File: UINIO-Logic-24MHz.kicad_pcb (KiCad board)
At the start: 2 copper layers, 52 x 25.4 mm, 55 parts, among them J1 Conn_01x10_Pin, U1 AT24CS64-XHM, U2 74HC245C, U3 ME6211C33M5G-N, U4 CY7C68013A-56LTX, Y1 24MHz

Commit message: update hardware
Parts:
- removed F1: 60V 1A, Fuse:Fuse_1206_3216Metric
- removed HOLE1, HOLE2, HOLE3, HOLE4: Hole-2mm, Uinio:Hole-2mm
- removed J1: Conn_01x10_Pin, Connector_PinHeader_2.54mm:PinHeader_1x10_P2.54mm_Vertical
- removed Y1: 24MHz, Crystal:Crystal_SMD_3225-4Pin_3.2x2.5mm
- added Y2: Crystal, Crystal:Crystal_SMD_HC49-SD, F.Cu at (143.8, 57.0)
- U1: footprint Package_SO:TSSOP-8_4.4x3mm_P0.65mm -> Package_SO:SO-8_3.9x4.9mm_P1.27mm
- U3: value ME6211C33M5G-N -> AP2127N-3.3; footprint Uinio:SOT-23-5_L3.0-W1.7-P0.95-LS2.8-BR -> Package_TO_SOT_SMD:SOT-23
- moved R1 57.5 mm to (137.9, 61.4)
- moved R13 56.7 mm to (143.7, 61.4), turned to 0 degrees
- moved R14 55.2 mm to (143.7, 63.4), turned to 0 degrees
- moved C1 55.2 mm to (150.1, 61.6), turned to 0 degrees
- moved R2 54.6 mm to (137.9, 63.4)
- moved R15 53.8 mm to (143.7, 65.3), turned to 0 degrees
- moved R16 52.5 mm to (143.7, 67.3), turned to 0 degrees
- moved D5 52.0 mm to (159.6, 61.6), turned to 0 degrees
- moved C2 51.7 mm to (150.1, 64.1), turned to 0 degrees
- moved R3 51.7 mm to (137.9, 65.3)
- moved C3 50.5 mm to (153.5, 61.4)
- moved D1 49.8 mm to (158.4, 71.7), turned to 0 degrees
- moved R4 48.9 mm to (137.9, 67.3)
- moved R7 48.4 mm to (140.8, 61.4)
- moved R17 48.0 mm to (143.7, 69.3)
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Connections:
- C2 pad 2: Net-(U3-Vout) -> +3.3V
- R1 pad 2: Net-(J1-Pin_9) -> unconnected-(R1-Pad2)
- R2 pad 2: Net-(J1-Pin_8) -> unconnected-(R2-Pad2)
- R3 pad 2: Net-(J1-Pin_7) -> unconnected-(R3-Pad2)
- R4 pad 2: Net-(J1-Pin_6) -> unconnected-(R4-Pad2)
- R5 pad 2: Net-(J1-Pin_5) -> unconnected-(R5-Pad2)
- R6 pad 2: Net-(J1-Pin_4) -> unconnected-(R6-Pad2)
- R7 pad 2: Net-(J1-Pin_3) -> unconnected-(R7-Pad2)
- R8 pad 2: Net-(J1-Pin_2) -> unconnected-(R8-Pad2)
- U3 pad 1: +5V -> GND
- U3 pad 2: GND -> +3.3V
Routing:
- net +3.3V: track 167.8 -> 0.00 mm, vias 12 -> 0
- net /USB_Data-: track 29.3 -> 0.00 mm
- net /USB_Data+: track 27.9 -> 0.00 mm, vias 2 -> 0
- net GND: track 24.0 -> 0.00 mm, vias 59 -> 0
- net Net-(U4-XTALIN): track 24.0 -> 0.00 mm
- net Net-(U4-XTALOUT): track 19.4 -> 0.00 mm
- net /INPUT4: track 16.8 -> 0.00 mm, vias 2 -> 0
- net /INPUT3: track 15.8 -> 0.00 mm, vias 2 -> 0
- net /INPUT5: track 15.3 -> 0.00 mm, vias 2 -> 0
- net /INPUT2: track 15.0 -> 0.00 mm, vias 2 -> 0
- net /INPUT6: track 14.4 -> 0.00 mm, vias 2 -> 0
- net /INPUT1: track 14.4 -> 0.00 mm, vias 2 -> 0
- net /INPUT7: track 13.4 -> 0.00 mm, vias 2 -> 0
- net /INPUT8: track 12.5 -> 0.00 mm, vias 2 -> 0
- net Net-(U4-PA0/~{INT0}): track 12.2 -> 0.00 mm
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- removed copper zone on B.Cu, net +3.3V
- removed copper zone on F.Cu, net +3.3V
- removed copper zone on B.Cu, net +5V
- removed copper zone on F.Cu, net +5V
- removed copper zone on F.Cu, net Net-(U3-Vout)
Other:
- board text removed: "CH0"
- board text removed: "CH1"
- board text removed: "CH2"
- board text removed: "CH3"
- board text removed: "CH4"
- board text removed: "CH5"
- board text removed: "CH6"
- board text removed: "CH7"
- board text removed: "GND"
- board text removed: "PA0"
- board text removed: "PA1"
- board text removed: "Power"
- board text removed: "UINIO Logic 24MHz"
- board text removed: "UINIO-Logic-24MHz"
- board text removed: "UinIO.com"
- board text removed: "Version 5.0.0"

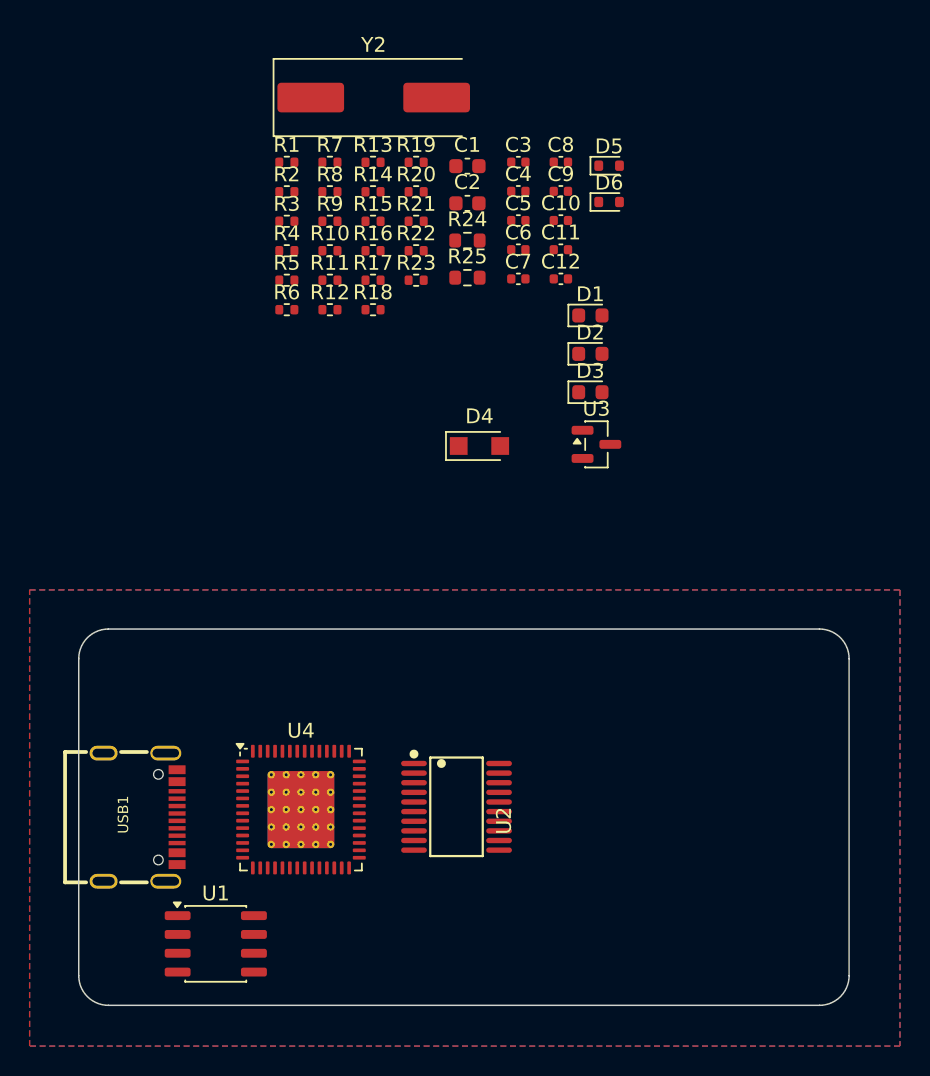
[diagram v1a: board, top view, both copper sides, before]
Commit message: update sch & brd with saleae clone hardware
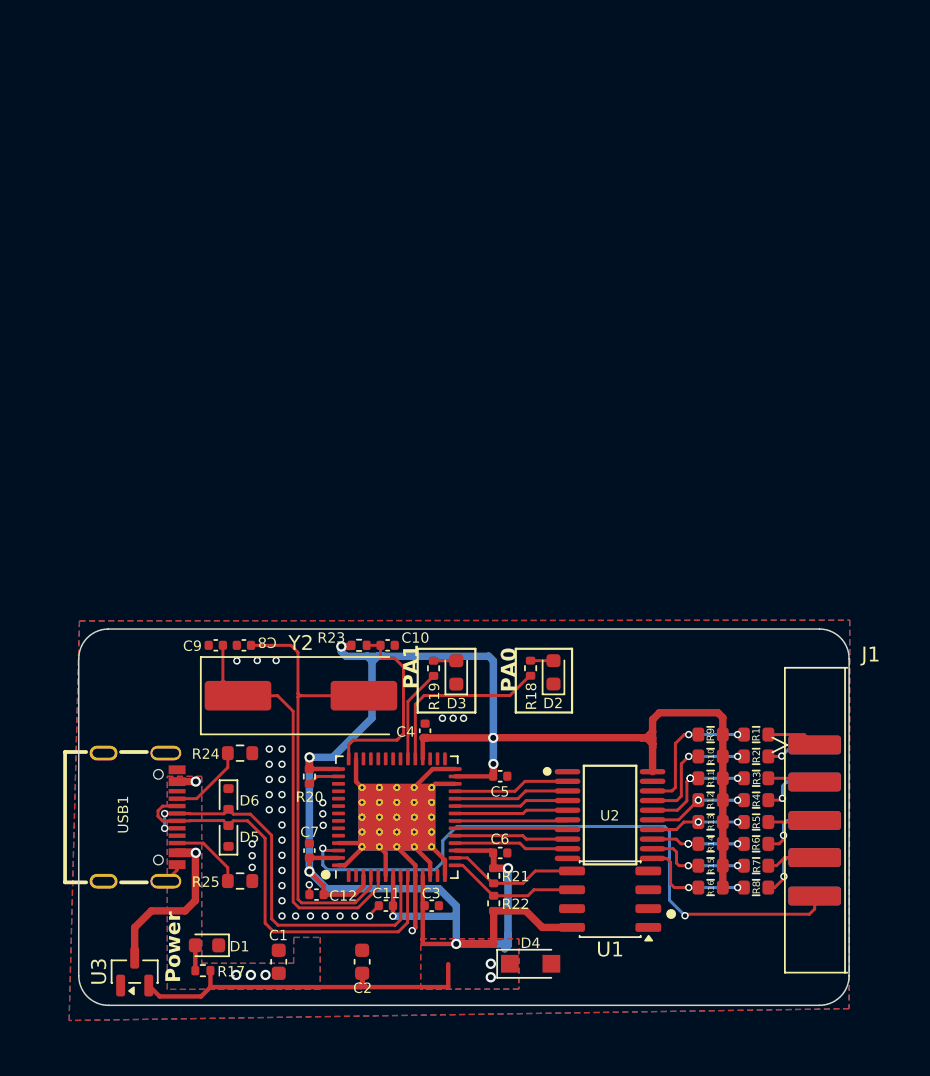
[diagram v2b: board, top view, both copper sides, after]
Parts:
- added J1: Conn_01x10_Pin, Uinio:IDC-Header_2x05_P2.54mm_EdgeMount, F.Cu at (171.1, 100.7)
- R1, R10, R11, R12, R13, R14, R15, R16, R2, R3, R4, R5, R6, R7, R8, R9: footprint Resistor_SMD:R_0402_1005Metric -> Resistor_SMD:R_0603_1608Metric
- moved R7 55.5 mm to (169.6, 108.8), turned to 180 degrees
- moved C1 55.2 mm to (137.3, 115.3), turned to -90 degrees
- moved R8 55.1 mm to (169.6, 110.3), turned to 180 degrees
- moved D5 52.0 mm to (133.9, 106.8), turned to 90 degrees
- moved C2 51.7 mm to (143.0, 115.3), turned to -90 degrees
- moved C3 50.5 mm to (147.7, 111.5)
- moved R13 50.0 mm to (166.5, 105.9)
- moved R1 50.0 mm to (169.6, 100.0), turned to 180 degrees
- moved D1 49.8 mm to (132.5, 114.2), turned to 180 degrees
- moved R14 49.6 mm to (166.5, 107.4)
- moved R2 49.6 mm to (169.6, 101.5), turned to 180 degrees
- moved R3 49.2 mm to (169.6, 103.0), turned to 180 degrees
- moved R15 49.1 mm to (166.5, 108.8)
- moved R4 48.8 mm to (169.6, 104.4), turned to 180 degrees
- moved R16 48.7 mm to (166.5, 110.3)
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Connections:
- R1 pad 1: /INPUT8 -> Net-(J1-Pin_1)
- R1 pad 2: unconnected-(R1-Pad2) -> /INPUT1
- R10 pad 1: +3.3V -> /INPUT2
- R10 pad 2: /INPUT2 -> +3.3V
- R11 pad 1: +3.3V -> /INPUT3
- R11 pad 2: /INPUT3 -> +3.3V
- R12 pad 1: +3.3V -> /INPUT4
- R12 pad 2: /INPUT4 -> +3.3V
- R13 pad 1: +3.3V -> /INPUT5
- R13 pad 2: /INPUT5 -> +3.3V
- R14 pad 1: +3.3V -> /INPUT6
- R14 pad 2: /INPUT6 -> +3.3V
- R15 pad 1: +3.3V -> /INPUT7
- R15 pad 2: /INPUT7 -> +3.3V
- R16 pad 1: +3.3V -> /INPUT8
- R16 pad 2: /INPUT8 -> +3.3V
- R2 pad 1: /INPUT7 -> Net-(J1-Pin_2)
- R2 pad 2: unconnected-(R2-Pad2) -> /INPUT2
- R3 pad 1: /INPUT6 -> Net-(J1-Pin_3)
- R3 pad 2: unconnected-(R3-Pad2) -> /INPUT3
- R4 pad 1: /INPUT5 -> Net-(J1-Pin_4)
- R4 pad 2: unconnected-(R4-Pad2) -> /INPUT4
- R5 pad 1: /INPUT4 -> Net-(J1-Pin_5)
- R5 pad 2: unconnected-(R5-Pad2) -> /INPUT5
- R6 pad 1: /INPUT3 -> Net-(J1-Pin_6)
- R6 pad 2: unconnected-(R6-Pad2) -> /INPUT6
- R7 pad 1: /INPUT2 -> Net-(J1-Pin_7)
- R7 pad 2: unconnected-(R7-Pad2) -> /INPUT7
- R8 pad 1: /INPUT1 -> Net-(J1-Pin_8)
- R8 pad 2: unconnected-(R8-Pad2) -> /INPUT8
- R9 pad 1: +3.3V -> /INPUT1
- R9 pad 2: /INPUT1 -> +3.3V
- U4 pad 54: unconnected-(U4-CLKOUT-Pad54) -> /CLK
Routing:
- net +3.3V: track 0.00 -> 169.1 mm, vias 0 -> 10
- net /CLK: track 0.00 -> 43.9 mm, vias 0 -> 2
- net Net-(U4-XTALOUT): track 0.00 -> 31.1 mm
- net /USB_Data-: track 0.00 -> 29.3 mm
- net Net-(U4-XTALIN): track 0.00 -> 28.2 mm
- net /USB_Data+: track 0.00 -> 27.9 mm, vias 0 -> 2
- net GND: track 0.00 -> 27.1 mm, vias 0 -> 37
- net Net-(U4-~{RESET}): track 0.00 -> 13.0 mm
- net +5V: track 0.00 -> 12.6 mm, vias 0 -> 5
- net Net-(U4-PA0/~{INT0}): track 0.00 -> 12.2 mm
- net /INPUT1: track 0.00 -> 10.8 mm, vias 0 -> 2
- net /INPUT2: track 0.00 -> 9.35 mm, vias 0 -> 2
- net /I2C_SDA: track 0.00 -> 8.88 mm
- net /I2C_SCL: track 0.00 -> 8.87 mm
- net /INPUT8: track 0.00 -> 8.48 mm, vias 0 -> 2
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- added copper zone on B.Cu, net +3.3V
- added copper zone on F.Cu, net +3.3V
- added copper zone on B.Cu, net +5V
- added copper zone on F.Cu, net +5V
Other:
- board text added: "PA0"
- board text added: "PA1"
- board text added: "Power"

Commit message: fix some routing
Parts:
- removed C12: 0.1uF, Capacitor_SMD:C_0402_1005Metric
- removed D4: 1N4007, Diode_SMD:Nexperia_CFP3_SOD-123W
- added JP1: ~, Uinio:SolderJumper-2_Open_RoundedPad_small, F.Cu at (149.2, 101.8)
- added JP10: ~, Uinio:SolderJumper-2_Open_RoundedPad_small, F.Cu at (139.8, 113.5)
- added JP2: ~, Uinio:SolderJumper-2_Open_RoundedPad_small, F.Cu at (149.2, 102.5)
- added JP3: ~, Uinio:SolderJumper-2_Open_RoundedPad_small, F.Cu at (149.2, 103.2)
- added JP4: ~, Uinio:SolderJumper-2_Open_RoundedPad_small, F.Cu at (149.2, 103.9)
- added JP5: ~, Uinio:SolderJumper-2_Open_RoundedPad_small, F.Cu at (149.2, 104.6)
- added JP6: ~, Uinio:SolderJumper-2_Open_RoundedPad_small, F.Cu at (149.2, 105.3)
- added JP7: ~, Uinio:SolderJumper-2_Open_RoundedPad_small, F.Cu at (149.2, 106.0)
- added JP8: ~, Uinio:SolderJumper-2_Open_RoundedPad_small, F.Cu at (149.2, 106.7)
- added JP9: ~, Uinio:SolderJumper-2_Open_RoundedPad_small, F.Cu at (139.8, 112.8)
- C10, C11, C3, C4, C5, C6, C7, C8, C9: footprint Capacitor_SMD:C_0402_1005Metric -> Capacitor_SMD:C_0603_1608Metric
- D1, D2, D3: footprint LED_SMD:LED_0603_1608Metric -> LED_SMD:LED_0805_2012Metric
- D5, D6: moved to B.Cu
- R17, R18, R19, R20, R21, R22, R23: footprint Resistor_SMD:R_0402_1005Metric -> Resistor_SMD:R_0603_1608Metric
- U4: footprint Package_DFN_QFN:QFN-56-1EP_8x8mm_P0.5mm_EP4.5x5.2mm_ThermalVias_TopTented -> Package_DFN_QFN:QFN-56-1EP_8x8mm_P0.5mm_EP4.5x5.2mm_ThermalVias
- USB1: footprint Uinio:USB-C-SMD_TYPEC-304J-BCP16 -> Connector_USB:USB_C_Receptacle_GCT_USB4105-xx-A_16P_TopMnt_Horizontal
- Y2: footprint Crystal:Crystal_SMD_HC49-SD -> Crystal:Crystal_HC49-4H_Vertical
- moved C5 19.8 mm to (132.6, 100.8), turned to 90 degrees
- moved C3 15.4 mm to (141.3, 97.6), turned to -90 degrees
- moved R21 12.4 mm to (141.1, 115.6), turned to 90 degrees
- moved U1 11.3 mm to (148.9, 114.5)
- moved R22 10.1 mm to (142.7, 115.6)
- moved U2 9.89 mm to (149.8, 104.9)
- moved R1 9.88 mm to (159.7, 99.6)
- moved R11 9.88 mm to (156.6, 102.5)
- moved R13 9.88 mm to (156.6, 105.5)
- moved R14 9.88 mm to (156.6, 107.0)
- moved R16 9.88 mm to (156.6, 109.9)
- moved R3 9.88 mm to (159.7, 102.5)
- moved R5 9.88 mm to (159.7, 105.5)
- moved R6 9.88 mm to (159.7, 107.0)
- moved R8 9.88 mm to (159.7, 109.9)
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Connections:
- R21 pad 2: /I2C_SDA -> Net-(JP10-A)
- R22 pad 2: /I2C_SCL -> Net-(JP9-A)
- U1 pad 5: /I2C_SDA -> Net-(JP9-A)
- U1 pad 6: /I2C_SCL -> Net-(JP10-A)
- U2 pad 2: /PB7 -> /PB0
- U2 pad 3: /PB6 -> /PB1
- U2 pad 4: /PB5 -> /PB2
- U2 pad 5: /PB4 -> /PB3
- U2 pad 6: /PB3 -> /PB4
- U2 pad 7: /PB2 -> /PB5
- U2 pad 8: /PB1 -> /PB6
- U2 pad 9: /PB0 -> /PB7
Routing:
- net +3.3V: track 169.1 -> 60.8 mm, vias 10 -> 7
- net /CLK: track 43.9 -> 0.00 mm, vias 2 -> 0
- net GND: track 27.1 -> 0.00 mm, vias 37 -> 0
- net /USB_Data-: track 29.3 -> 6.79 mm
- net /USB_Data+: track 27.9 -> 6.39 mm
- net Net-(U4-XTALOUT): track 31.1 -> 13.5 mm
- net /PB0: track 7.74 -> 20.9 mm
- net Net-(U4-XTALIN): track 28.2 -> 15.4 mm
- net /PB1: track 7.68 -> 19.8 mm, vias 0 -> 2
- net /PB2: track 7.62 -> 17.3 mm, vias 0 -> 2
- net /PB3: track 7.61 -> 17.1 mm, vias 0 -> 2
- net Net-(U4-PA1/~{INT1}): track 6.31 -> 15.8 mm
- net Net-(JP9-A): track 0.00 -> 8.94 mm, vias 0 -> 2
- net Net-(U4-PA0/~{INT0}): track 12.2 -> 20.9 mm
- net Net-(JP10-A): track 0.00 -> 8.48 mm
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- removed copper zone on B.Cu, net +3.3V
- removed copper zone on F.Cu, net +3.3V
- removed copper zone on B.Cu, net +5V
- removed copper zone on F.Cu, net +5V
- removed copper zone on B.Cu, net GND
- removed copper zone on F.Cu, net GND
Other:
- board size 52 x 25.4 mm -> 43.4 x 25.4 mm
- board text removed: "Power"

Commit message: update routing
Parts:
- JP10, JP9: footprint Uinio:SolderJumper-2_Open_RoundedPad_small -> Uinio:SolderJumper-2_Bridged2Bar_RoundedPad_small
- USB1: footprint Connector_USB:USB_C_Receptacle_GCT_USB4105-xx-A_16P_TopMnt_Horizontal -> Uinio:USB-C-SMD_TYPEC-304J-BCP16
- moved C10 1.52 mm to (147.8, 97.6)
- moved R23 1.27 mm to (145.9, 97.6)
- moved USB1 1.10 mm to (127.9, 105.6)
- moved R20 1.02 mm to (144.0, 97.6)
- moved C3 0.76 mm to (142.1, 97.6)
- moved R24 0.08 mm to (132.5, 103.8)
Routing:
- net +3.3V: track 60.8 -> 131.3 mm, vias 7 -> 11
- net /CLK: track 0.00 -> 44.7 mm, vias 0 -> 2
- net GND: track 0.00 -> 27.8 mm, vias 0 -> 75
- net /INPUT3: track 4.46 -> 11.3 mm, vias 0 -> 2
- net /INPUT5: track 3.25 -> 10.0 mm, vias 0 -> 2
- net /INPUT1: track 6.18 -> 12.9 mm, vias 0 -> 2
- net /INPUT2: track 5.54 -> 12.3 mm, vias 0 -> 2
- net /INPUT4: track 3.59 -> 10.3 mm, vias 0 -> 2
- net /INPUT8: track 4.41 -> 11.1 mm, vias 0 -> 2
- net /INPUT6: track 3.28 -> 9.93 mm, vias 0 -> 2
- net /INPUT7: track 3.63 -> 10.3 mm, vias 0 -> 2
- net /PB0: track 20.9 -> 23.4 mm
- net /PB1: track 19.8 -> 22.3 mm
- net /PB2: track 17.3 -> 19.8 mm
- net /PB3: track 17.1 -> 19.5 mm
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- added copper zone on F.Cu, net +3.3V
- added copper zone on B.Cu, net GND
- added copper zone on F.Cu, net GND
